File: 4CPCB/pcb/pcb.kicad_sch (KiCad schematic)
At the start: 44 parts, among them J1 Conn_01x04, J14 Conn_01x04, J15 Conn_01x04, J16 Conn_01x04, J17 Conn_01x04, J18 Conn_01x04, J19 Conn_01x04, J2 XT90PW-F, J20 Conn_01x04, J21 Conn_01x04, J22 Conn_01x03, J23 Conn_01x04, J24 Conn_01x10, J3 Conn_01x04, J4 Conn_01x02, J5 Conn_01x03, J6 Conn_01x03, J7 Conn_01x03, J8 Conn_01x03, J9 Conn_01x03, U5 STM32G474RETx, U6 AMS1117-3.3, U7 SN65HVD230DR

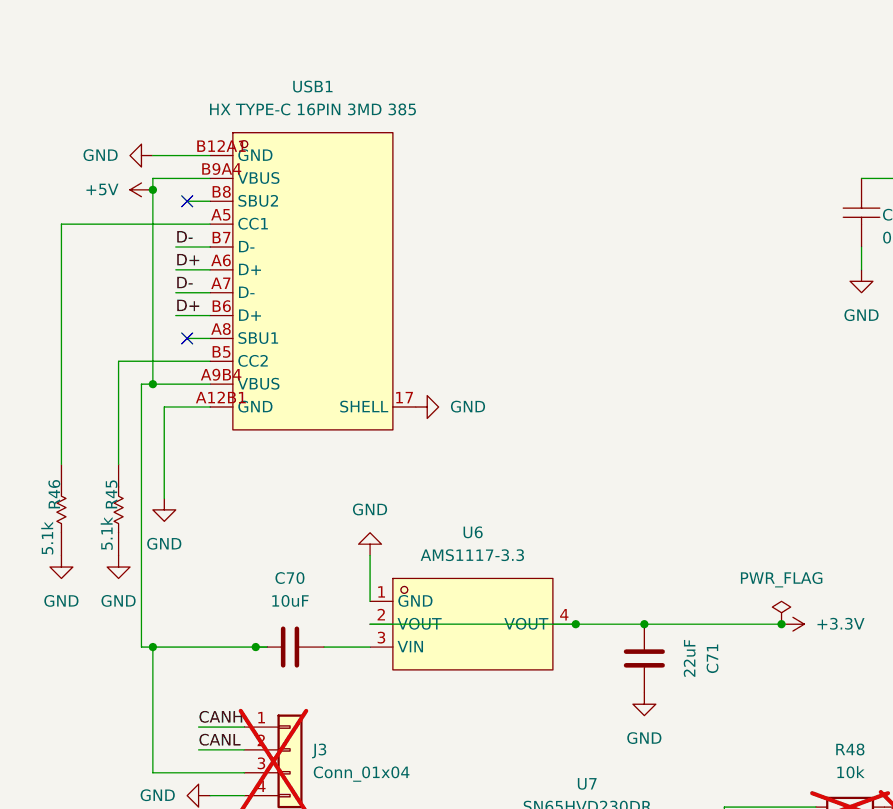
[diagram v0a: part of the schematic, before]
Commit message: Add project-local KiCad libraries
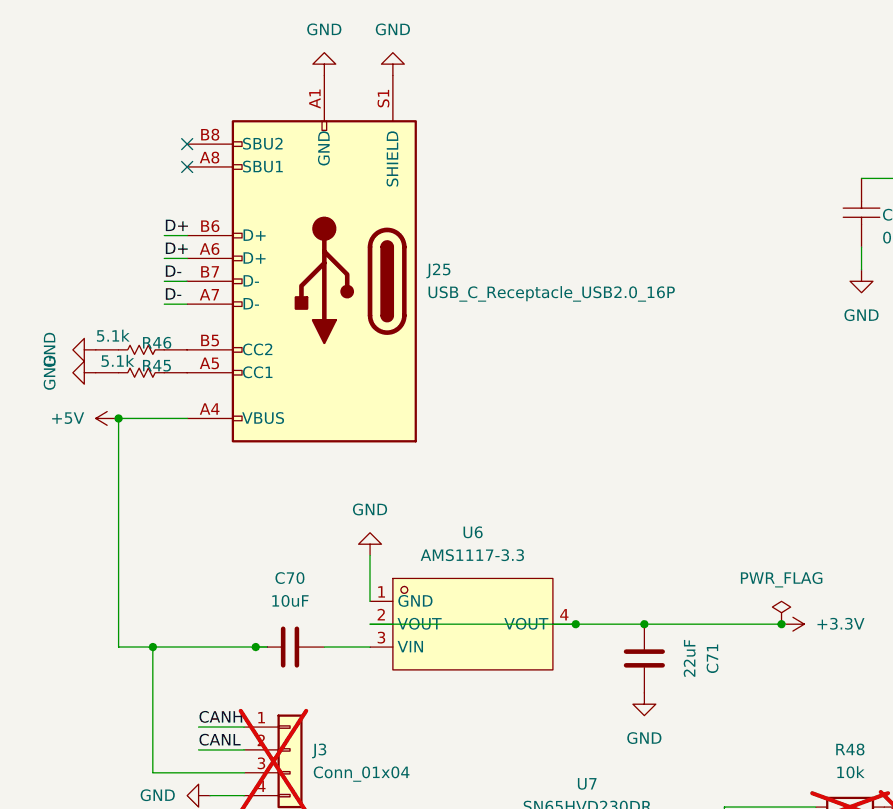
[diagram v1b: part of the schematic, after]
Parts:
- removed USB1: HX TYPE-C 16PIN 3MD 385, Easyeda:TYPE-C-SMD_HX-TYPE-C-16PIN, symbol EasyEda2KiCad:HXTYPE-C16PIN3MD385
- added J25: USB_C_Receptacle_USB2.0_16P, Connector_USB:USB_C_Receptacle_HRO_TYPE-C-31-M-12, symbol Connector:USB_C_Receptacle_USB2.0_16P
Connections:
- net +5V: now also J25.A4 (VBUS), J25.A9 (VBUS), J25.B4 (VBUS), J25.B9 (VBUS)
- net D+: now also J25.A6 (D+), J25.B6 (D+)
- net D-: now also J25.A7 (D-), J25.B7 (D-)
- net GND: now also J25.A1 (GND), J25.A12 (GND), J25.B1 (GND), J25.B12 (GND), J25.S1 (SHIELD)
- net at R46.1: now also J25.B5 (CC2)
- net at R45.1: now also J25.A5 (CC1)
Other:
- moved on the sheet: R45, R46
